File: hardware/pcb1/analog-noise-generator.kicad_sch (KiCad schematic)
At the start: 89 parts, among them J1 USB_C_Receptacle_USB2.0, J2 Conn_01x03_Pin, J3 PJ-211A, J4 PJ-211A, J5 Conn_01x04_Pin, J6 Conn_01x04_Pin, J7 Conn_01x02_Pin, J9 Conn_02x04_Odd_Even, U1 STM32F072CBTx, U2 USBLC6-2SC6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

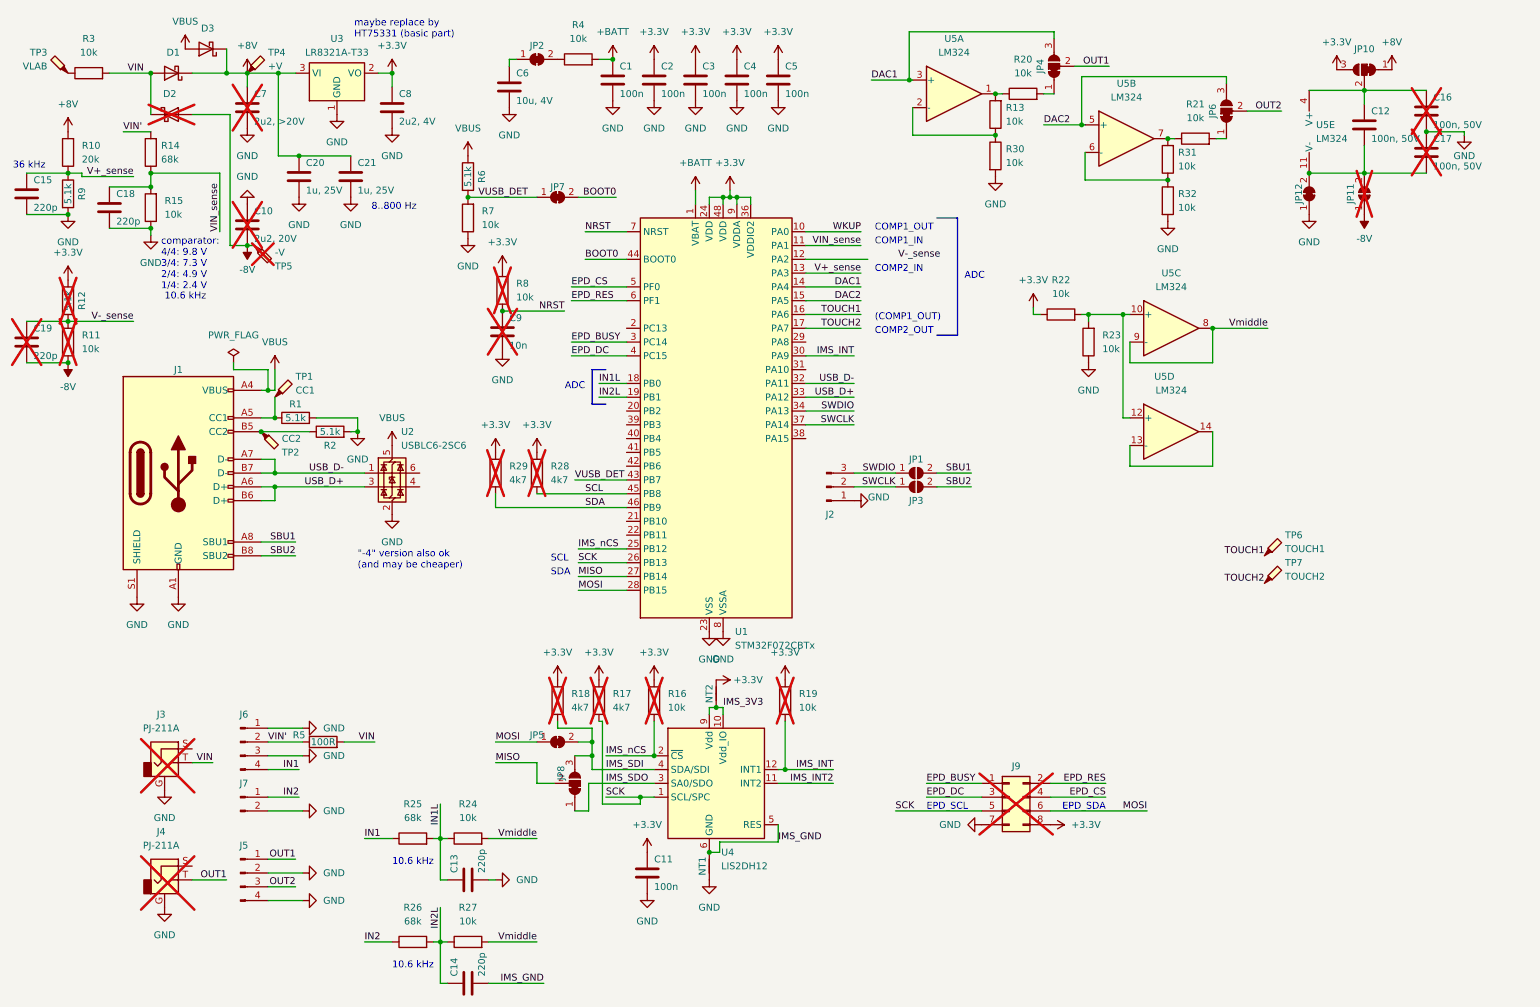
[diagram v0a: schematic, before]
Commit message: fix ERC issues
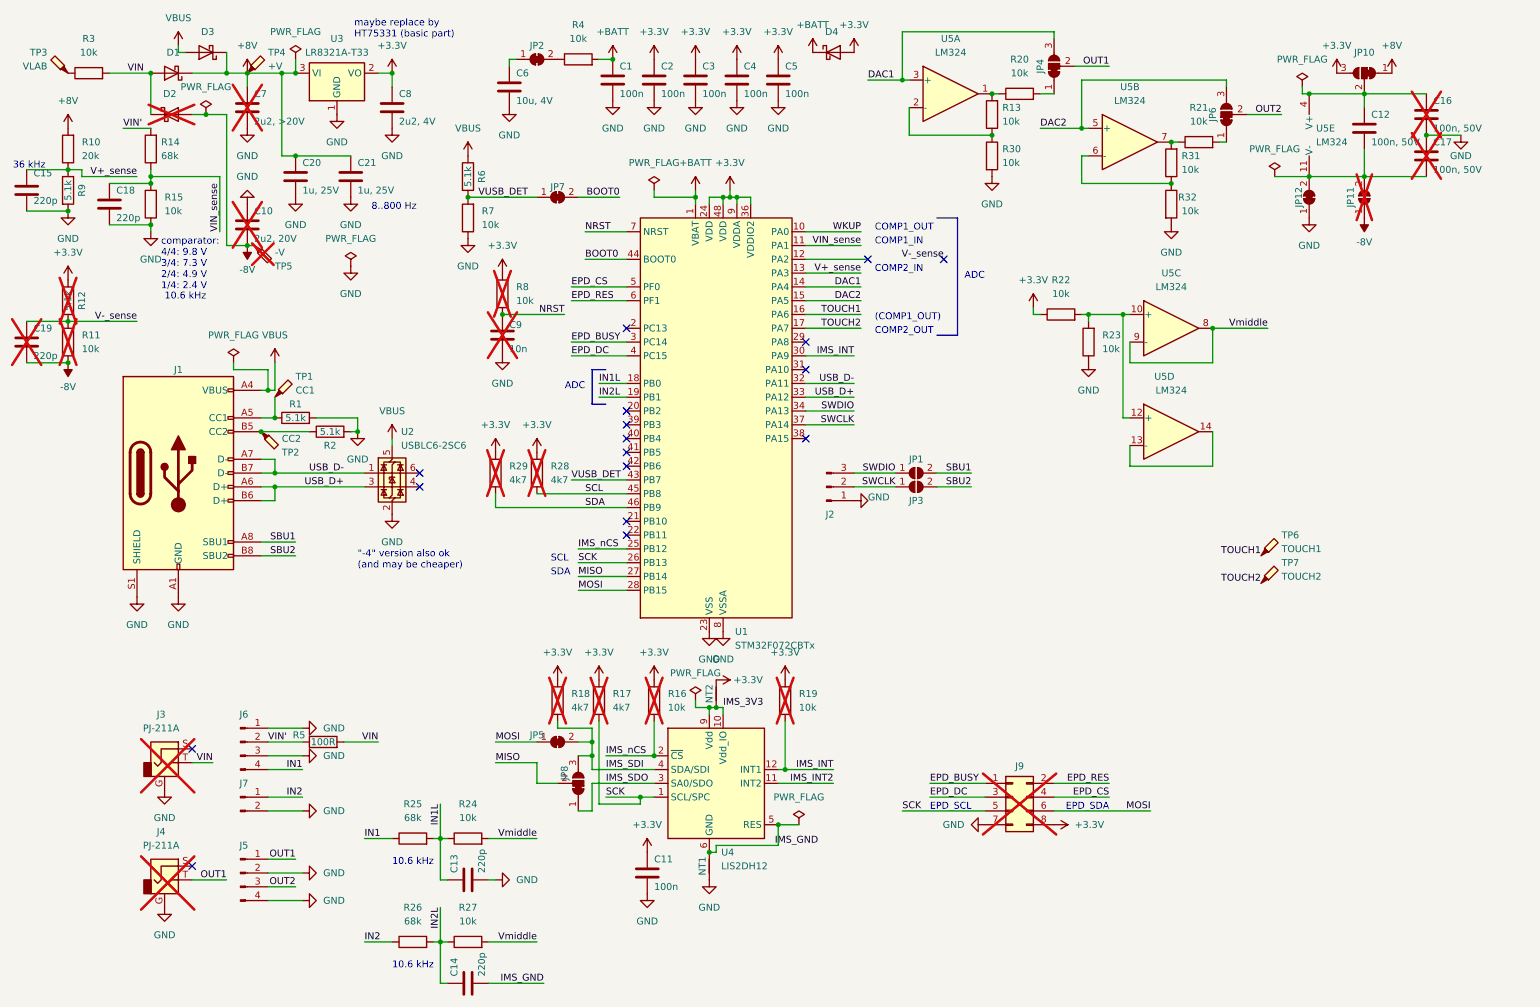
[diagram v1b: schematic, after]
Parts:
- added D4: ~, Diode_SMD:D_SOD-323, symbol Device:D_Schottky
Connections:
- net +3.3V: now also D4.2 (A)
- net +BATT: now also D4.1 (K)
- no-connect marks 0 -> 17
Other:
- moved on the sheet: C12, C15, C16, C17, C18, C20, C9, D3, J9, JP10, JP11, JP12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

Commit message: generate files for JLC
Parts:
- J3, J4, J5, J6, J7, J9: DNP (none) -> PCBA
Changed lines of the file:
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@@
       (effects (font (size 1.27 1.27)) hide)
     )
+    (property "DNP" "PCBA" (at 54.61 146.05 0)
+      (effects (font (size 1.27 1.27)) hide)
+    )
     (pin "2")
     (pin "3")
@@
       (effects (font (size 1.27 1.27)) hide)
     )
+    (property "DNP" "PCBA" (at 54.61 170.18 0)
+      (effects (font (size 1.27 1.27)) hide)
+    )
     (pin "2")
     (pin "3")
@@
       (effects (font (size 1.27 1.27)) hide)
     )
+    (property "DNP" "PCBA" (at 54.61 156.21 0)
+      (effects (font (size 1.27 1.27)) hide)
+    )
     (pin "2")
     (pin "1")
@@
       (effects (font (size 1.27 1.27)) hide)
     )
+    (property "DNP" "PCBA" (at 40.64 149.86 0)
+      (effects (font (size 1.27 1.27)) hide)
+    )
     (pin "S")
     (pin "T")
@@
       (effects (font (size 1.27 1.27)) hide)
     )
+    (property "DNP" "PCBA" (at 40.64 171.45 0)
+      (effects (font (size 1.27 1.27)) hide)
+    )
     (pin "S")
     (pin "T")
@@
       (effects (font (size 1.27 1.27)) hide)
     )
+    (property "DNP" "PCBA" (at 196.85 156.21 0)
+      (effects (font (size 1.27 1.27)) hide)
+    )

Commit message: switch to four layers and continue routing
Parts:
- added TP8: TOUCH3, analog-noise-generator:TestPoint_THTPad_small, symbol Connector:TestPoint_Probe
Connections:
- net OUT1: now also R20.2; no longer JP4.2 (C)
- net OUT2: now also R21.2; no longer JP6.2 (C)
- net at R31.2, U5.7: now also JP6.1 (A); no longer R21.1
- net at R13.2, U5.1: now also JP4.1 (A); no longer R20.1
- net AVCC: now reaches C12.1, C16.1, JP10.2 (C), U5.4 (V+)
- net TOUCH3: now reaches U1.12 (PA2)
- net TOUCH3: now also TP8.1
- net AGND: now reaches C12.2, C17.2, JP11.2 (B), JP12.2 (B), U5.11 (V-)
- new net: JP6.2 (C), R21.1
- new net: JP4.2 (C), R20.1
- no-connect marks 17 -> 16
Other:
- moved on the sheet: JP4, JP6, R20, R21
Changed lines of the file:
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@@
   (no_connect (at 125.73 90.17))
   (no_connect (at 125.73 107.95))
-  (no_connect (at 170.18 57.15))
   (no_connect (at 125.73 95.25))
   (no_connect (at 184.15 57.15))
@@
     (stroke (width 0) (type default))
   )
-  (wire (pts (xy 204.47 15.24) (xy 176.53 15.24))
+  (wire (pts (xy 193.04 15.24) (xy 176.53 15.24))
     (stroke (width 0) (type default))
   )
@@
     (stroke (width 0) (type default))
   )
-  (wire (pts (xy 204.47 16.51) (xy 204.47 15.24))
+  (wire (pts (xy 193.04 16.51) (xy 193.04 15.24))
     (stroke (width 0) (type default))
   )
@@
     (stroke (width 0) (type default))
   )
+  (wire (pts (xy 205.74 21.59) (xy 210.82 21.59))
+    (stroke (width 0) (type default))
+  )
   (wire (pts (xy 182.88 99.06) (xy 189.23 99.06))
     (stroke (width 0) (type default))
@@
     (stroke (width 0) (type default))
   )
-  (wire (pts (xy 208.28 21.59) (xy 214.63 21.59))
+  (wire (pts (xy 196.85 21.59) (xy 198.12 21.59))
     (stroke (width 0) (type default))
   )
@@
     (stroke (width 0) (type default))
   )
-  (wire (pts (xy 234.95 35.56) (xy 236.22 35.56))
+  (wire (pts (xy 226.06 35.56) (xy 226.06 36.83))
     (stroke (width 0) (type default))
   )
@@
     (stroke (width 0) (type default))
   )
+  (wire (pts (xy 238.76 31.75) (xy 243.84 31.75))
+    (stroke (width 0) (type default))
+  )
   (wire (pts (xy 119.38 153.67) (xy 119.38 158.75))
     (stroke (width 0) (type default))
@@
     (stroke (width 0) (type default))
   )
-  (wire (pts (xy 226.06 35.56) (xy 227.33 35.56))
-    (stroke (width 0) (type default))
-  )
   (wire (pts (xy 153.67 161.29) (xy 157.48 161.29))
     (stroke (width 0) (type default))
@@
     (stroke (width 0) (type default))
   )
-  (wire (pts (xy 240.03 30.48) (xy 246.38 30.48))
+  (wire (pts (xy 229.87 31.75) (xy 231.14 31.75))
     (stroke (width 0) (type default))
   )
@@
     (stroke (width 0) (type default))
   )
-  (wire (pts (xy 236.22 24.13) (xy 209.55 24.13))
+  (wire (pts (xy 226.06 24.13) (xy 209.55 24.13))
     (stroke (width 0) (type default))
   )
@@
     (stroke (width 0) (type default))
   )
-  (wire (pts (xy 236.22 25.4) (xy 236.22 24.13))
+  (wire (pts (xy 226.06 26.67) (xy 226.06 24.13))
     (stroke (width 0) (type default))
   )
@@
     (stroke (width 0) (type default))
   )
-  (wire (pts (xy 158.75 57.15) (xy 170.18 57.15))
+  (wire (pts (xy 158.75 57.15) (xy 168.91 57.15))
     (stroke (width 0) (type default))
   )
@@
     (stroke (width 0) (type default))
   )
-  (wire (pts (xy 201.93 26.67) (xy 204.47 26.67))
-    (stroke (width 0) (type default))
-  )
   (wire (pts (xy 55.88 54.61) (xy 57.15 54.61))
     (stroke (width 0) (type default))
@@
     (stroke (width 0) (type default))
   )
-  (wire (pts (xy 193.04 26.67) (xy 194.31 26.67))
-    (stroke (width 0) (type default))
-  )
   (wire (pts (xy 193.04 34.29) (xy 177.8 34.29))
     (stroke (width 0) (type default))
@@
     (effects (font (size 1.27 1.27)) (justify left bottom))
   )
+  (label "TOUCH3" (at 168.91 57.15 180) (fields_autoplaced)
+    (effects (font (size 1.27 1.27)) (justify right bottom))
+  )
   (label "VIN_sense" (at 50.8 52.07 90) (fields_autoplaced)
     (effects (font (size 1.27 1.27)) (justify left bottom))
@@
     (effects (font (size 1.27 1.27)) (justify left bottom))
   )
+  (label "TOUCH3" (at 242.57 121.92 180) (fields_autoplaced)
+    (effects (font (size 1.27 1.27)) (justify right bottom))
+  )
   (label "VIN" (at 36.83 22.86 180) (fields_autoplaced)
     (effects (font (size 1.27 1.27)) (justify right bottom))
@@
     (effects (font (size 1.27 1.27)) (justify right bottom))
   )
-  (label "OUT2" (at 246.38 30.48 180) (fields_autoplaced)
+  (label "OUT2" (at 243.84 31.75 180) (fields_autoplaced)
     (effects (font (size 1.27 1.27)) (justify right bottom))
   )
@@
     (effects (font (size 1.27 1.27)) (justify right bottom))
   )
+  (label "AVCC" (at 252.73 26.67 0) (fields_autoplaced)
+    (effects (font (size 1.27 1.27)) (justify left bottom))
+  )
+  (label "AGND" (at 252.73 41.91 0) (fields_autoplaced)
+    (effects (font (size 1.27 1.27)) (justify left bottom))
+  )
   (label "IMS_INT2" (at 163.83 153.67 180) (fields_autoplaced)
     (effects (font (size 1.27 1.27)) (justify right bottom))
@@
     (effects (font (size 1.27 1.27)) (justify right bottom))
   )
-  (label "OUT1" (at 214.63 21.59 180) (fields_autoplaced)
+  (label "OUT1" (at 210.82 21.59 180) (fields_autoplaced)
     (effects (font (size 1.27 1.27)) (justify right bottom))
   )
@@
     )
   )
-  (symbol (lib_id "Device:R") (at 231.14 35.56 90) (unit 1)
+  (symbol (lib_id "Device:R") (at 234.95 31.75 90) (unit 1)
     (in_bom yes) (on_board yes) (dnp no) (fields_autoplaced)
-    (property "Reference" "R21" (at 231.14 29.21 90)
+    (property "Reference" "R21" (at 234.95 25.4 90)
       (effects (font (size 1.27 1.27)))
     )
-    (property "Value" "10k" (at 231.14 31.75 90)
+    (property "Value" "10k" (at 234.95 27.94 90)
       (effects (font (size 1.27 1.27)))
     )
-    (property "Footprint" "Resistor_SMD:R_0402_1005Metric" (at 231.14 37.338 90)
+    (property "Footprint" "Resistor_SMD:R_0402_1005Metric" (at 234.95 33.528 90)
       (effects (font (size 1.27 1.27)) hide)
     )
-    (property "Datasheet" "~" (at 231.14 35.56 0)
+    (property "Datasheet" "~" (at 234.95 31.75 0)
       (effects (font (size 1.27 1.27)) hide)
     )
-    (property "LCSC" "C25744" (at 231.14 35.56 0)
+    (property "LCSC" "C25744" (at 234.95 31.75 0)
       (effects (font (size 1.27 1.27)) hide)
     )
@@
     )
   )
-  (symbol (lib_id "Jumper:SolderJumper_3_Bridged12") (at 236.22 30.48 90) (unit 1)
+  (symbol (lib_id "Jumper:SolderJumper_3_Bridged12") (at 226.06 31.75 90) (unit 1)
     (in_bom yes) (on_board yes) (dnp no)
-    (property "Reference" "JP6" (at 233.68 30.48 0)
+    (property "Reference" "JP6" (at 223.52 31.75 0)
       (effects (font (size 1.27 1.27)))
     )
-    (property "Value" "SolderJumper_3_Bridged12" (at 234.315 31.75 90)
+    (property "Value" "SolderJumper_3_Bridged12" (at 224.155 33.02 90)
       (effects (font (size 1.27 1.27)) (justify left) hide)
     )
-    (property "Footprint" "Jumper:SolderJumper-3_P1.3mm_Bridged12_RoundedPad1.0x1.5mm" (at 236.22 30.48 0)
+    (property "Footprint" "Jumper:SolderJumper-3_P1.3mm_Bridged12_RoundedPad1.0x1.5mm" (at 226.06 31.75 0)
       (effects (font (size 1.27 1.27)) hide)
     )
-    (property "Datasheet" "~" (at 236.22 30.48 0)
+    (property "Datasheet" "~" (at 226.06 31.75 0)
       (effects (font (size 1.27 1.27)) hide)
     )
@@
     )
   )
-  (symbol (lib_id "Jumper:SolderJumper_3_Bridged12") (at 204.47 21.59 90) (unit 1)
+  (symbol (lib_id "Jumper:SolderJumper_3_Bridged12") (at 193.04 21.59 90) (unit 1)
     (in_bom yes) (on_board yes) (dnp no)
-    (property "Reference" "JP4" (at 201.93 21.59 0)
+    (property "Reference" "JP4" (at 190.5 21.59 0)
       (effects (font (size 1.27 1.27)))
     )
-    (property "Value" "SolderJumper_3_Bridged12" (at 202.565 22.86 90)
+    (property "Value" "SolderJumper_3_Bridged12" (at 191.135 22.86 90)
       (effects (font (size 1.27 1.27)) (justify left) hide)
     )
-    (property "Footprint" "Jumper:SolderJumper-3_P1.3mm_Bridged12_RoundedPad1.0x1.5mm" (at 204.47 21.59 0)
+    (property "Footprint" "Jumper:SolderJumper-3_P1.3mm_Bridged12_RoundedPad1.0x1.5mm" (at 193.04 21.59 0)
       (effects (font (size 1.27 1.27)) hide)
     )
-    (property "Datasheet" "~" (at 204.47 21.59 0)
+    (property "Datasheet" "~" (at 193.04 21.59 0)
       (effects (font (size 1.27 1.27)) hide)
     )
@@
     )
   )
+  (symbol (lib_id "Connector:TestPoint_Probe") (at 242.57 121.92 0) (unit 1)
+    (in_bom no) (on_board yes) (dnp no)
+    (property "Reference" "TP8" (at 246.38 118.11 0)
+      (effects (font (size 1.27 1.27)) (justify left))
+    )
+    (property "Value" "TOUCH3" (at 246.38 120.65 0)
+      (effects (font (size 1.27 1.27)) (justify left))
+    )
+    (property "Footprint" "analog-noise-generator:TestPoint_THTPad_small" (at 247.65 121.92 0)
+      (effects (font (size 1.27 1.27)) hide)
+    )
+    (property "Datasheet" "~" (at 247.65 121.92 0)
+      (effects (font (size 1.27 1.27)) hide)
+    )
+    (pin "1")
+    (instances
+      (project "analog-noise-generator"
+        (path "/e71fa5ad-0f80-45ec-aa84-70ffc489027a"
+          (reference "TP8") (unit 1)
+        )
+      )
+    )
+  )
   (symbol (lib_id "Device:C") (at 146.05 24.13 0) (unit 1)
     (in_bom yes) (on_board yes) (dnp no)
@@
     )
   )
-  (symbol (lib_id "Device:R") (at 198.12 26.67 90) (unit 1)
+  (symbol (lib_id "Device:R") (at 201.93 21.59 90) (unit 1)
     (in_bom yes) (on_board yes) (dnp no) (fields_autoplaced)
-    (property "Reference" "R20" (at 198.12 20.32 90)
+    (property "Reference" "R20" (at 201.93 15.24 90)
       (effects (font (size 1.27 1.27)))
     )
-    (property "Value" "10k" (at 198.12 22.86 90)
+    (property "Value" "10k" (at 201.93 17.78 90)
       (effects (font (size 1.27 1.27)))
     )
-    (property "Footprint" "Resistor_SMD:R_0402_1005Metric" (at 198.12 28.448 90)
+    (property "Footprint" "Resistor_SMD:R_0402_1005Metric" (at 201.93 23.368 90)
       (effects (font (size 1.27 1.27)) hide)
     )
-    (property "Datasheet" "~" (at 198.12 26.67 0)
+    (property "Datasheet" "~" (at 201.93 21.59 0)
       (effects (font (size 1.27 1.27)) hide)
     )
-    (property "LCSC" "C25744" (at 198.12 26.67 0)
+    (property "LCSC" "C25744" (at 201.93 21.59 0)
       (effects (font (size 1.27 1.27)) hide)
     )
